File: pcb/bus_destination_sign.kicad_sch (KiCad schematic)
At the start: 34 parts, among them J1 USB_C_Receptacle_USB2.0_16P, J2 Display Connector Input, J3 SSD1322 30-Pin Connector, U1 ESP32-S3-WROOM-1, U2 AP2112K-3.3, U3 MT3608

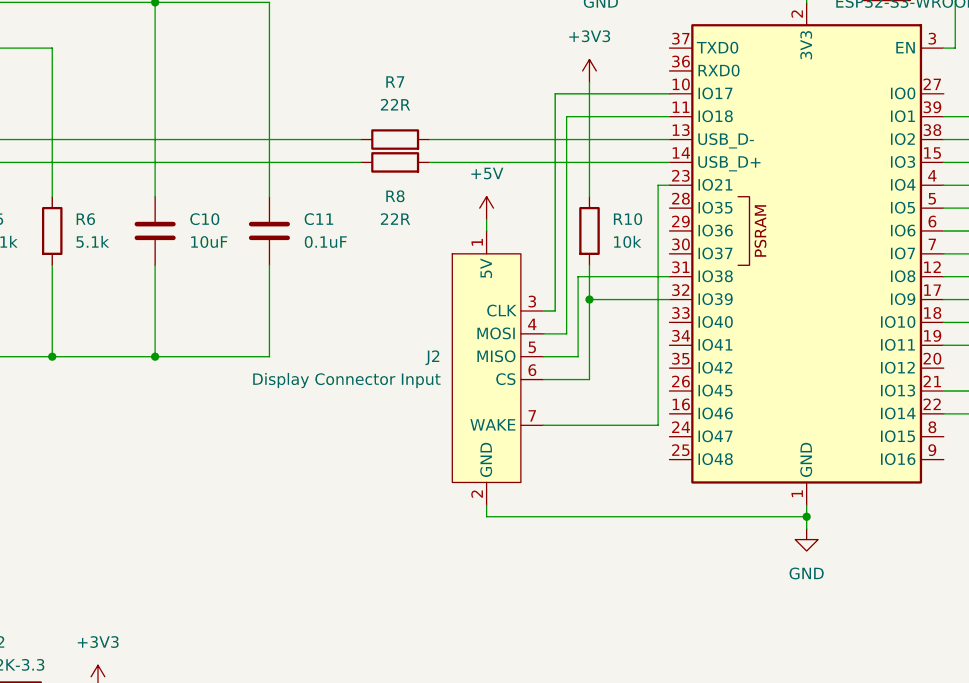
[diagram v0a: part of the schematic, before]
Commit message: Reroute SSD1322 PCB
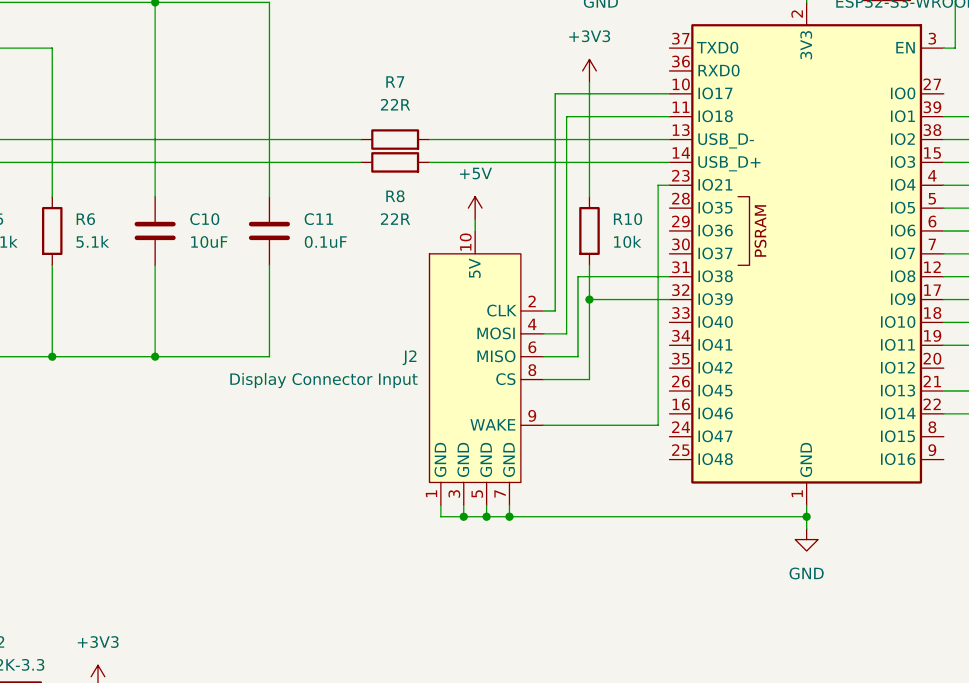
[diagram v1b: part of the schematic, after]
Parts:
- J2: footprint Connector_PinHeader_2.54mm:PinHeader_1x07_P2.54mm_Vertical -> Connector_IDC:IDC-Header_2x05_P2.54mm_Horizontal
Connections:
- net +5V: now also J2.10 (5V); no longer J2.1 (5V)
- net GND: now also J2.1 (GND), J2.3 (GND), J2.5 (GND), J2.7 (GND); no longer J2.2 (GND)
- net at R10.2, U1.32 (IO39): now also J2.8 (CS); no longer J2.6 (CS)
- net at U1.10 (IO17): now also J2.2 (CLK); no longer J2.3 (CLK)
- net at U1.31 (IO38): now also J2.6 (MISO); no longer J2.5 (MISO)
- net at U1.23 (IO21): now also J2.9 (WAKE); no longer J2.7 (WAKE)

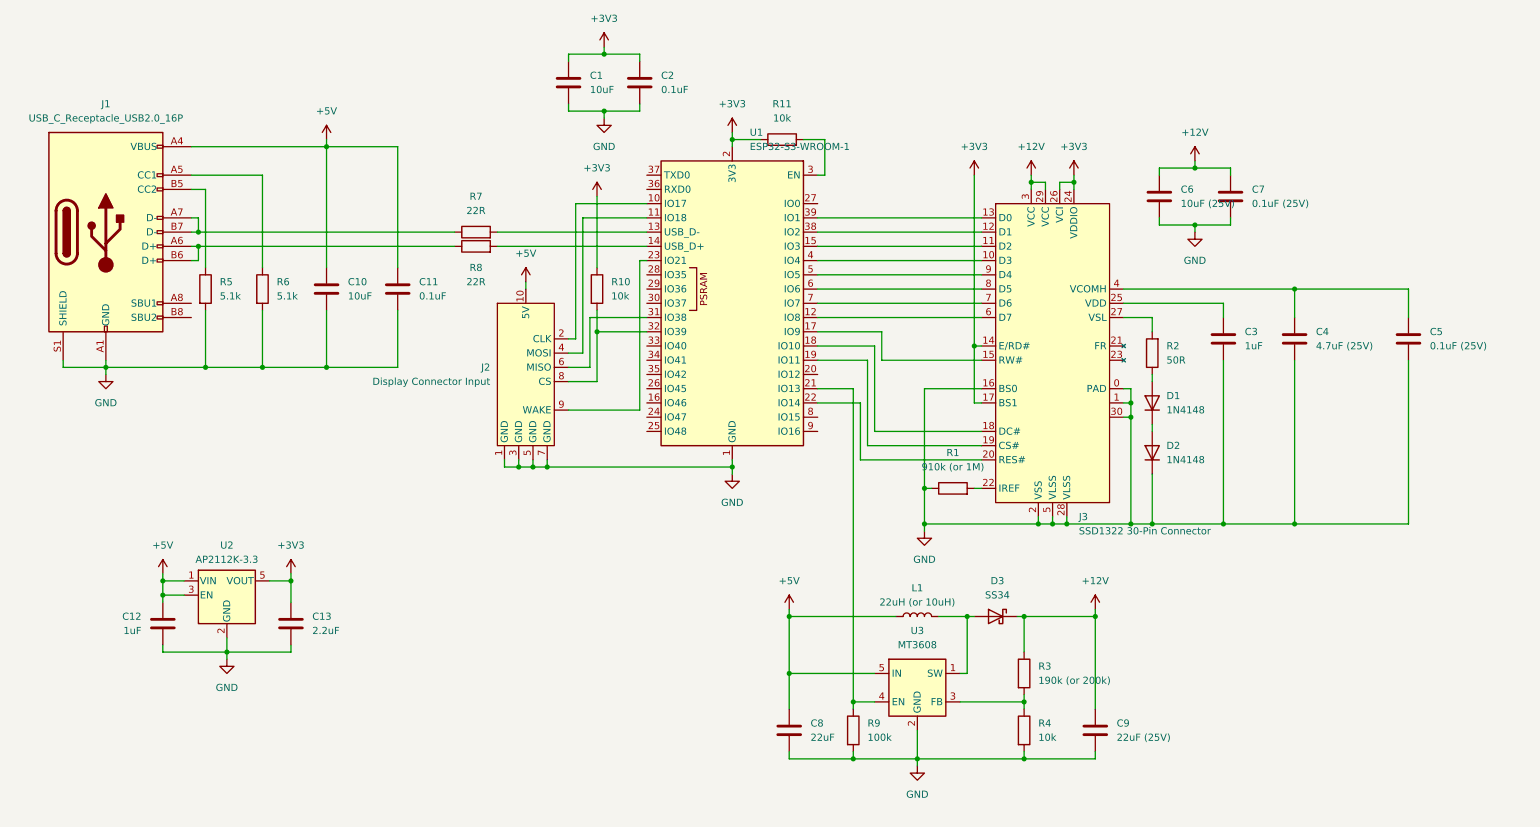
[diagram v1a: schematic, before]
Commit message: Added ESP32 master circuit
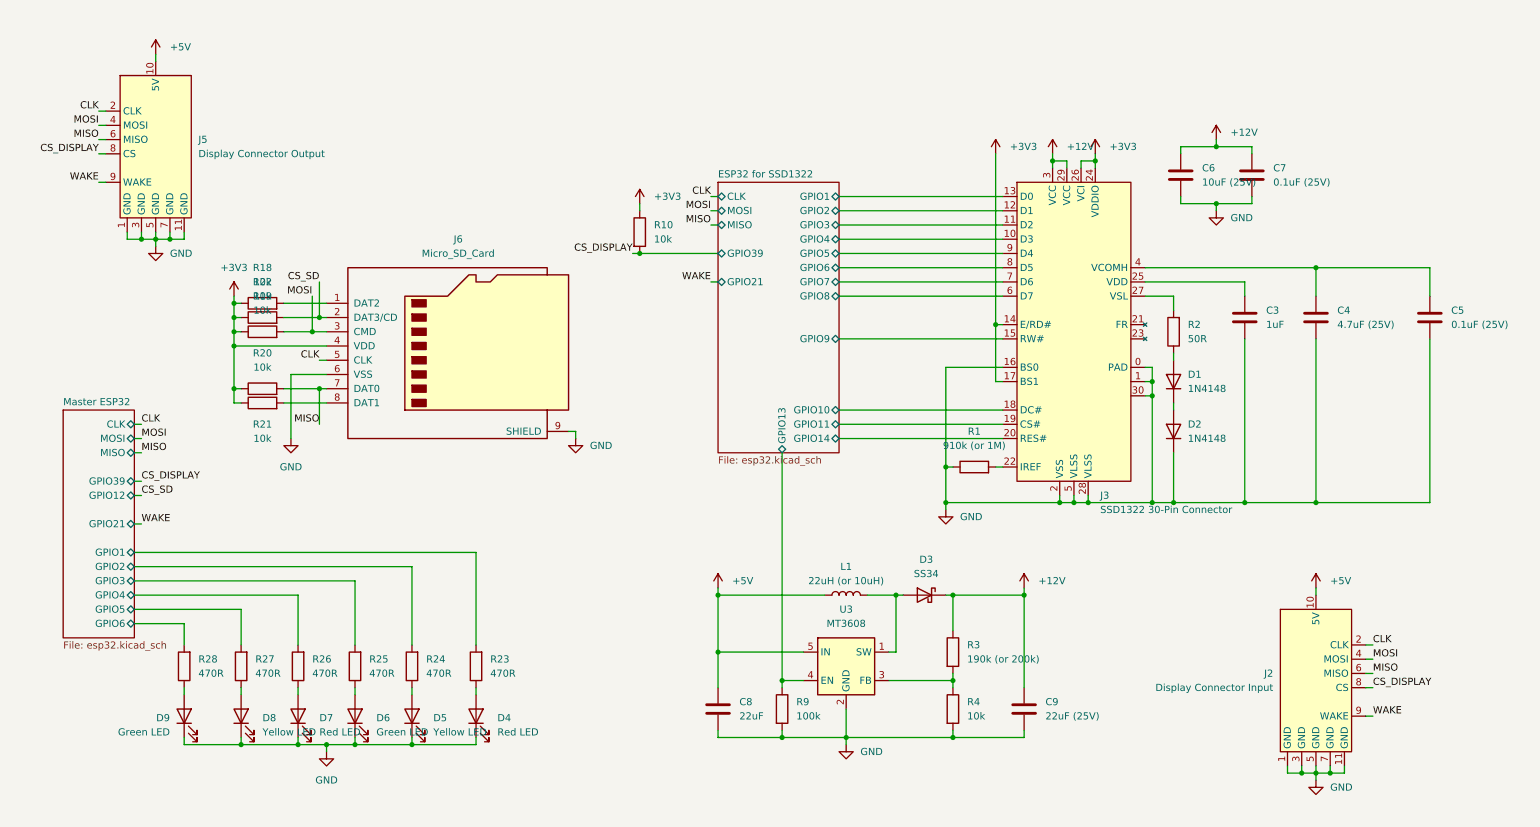
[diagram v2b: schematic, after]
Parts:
- removed C1, C10: 10uF, Capacitor_SMD:C_0603_1608Metric, symbol Device:C
- removed C11, C2: 0.1uF, Capacitor_SMD:C_0603_1608Metric, symbol Device:C
- removed C12: 1uF, Capacitor_SMD:C_0603_1608Metric, symbol Device:C
- removed C13: 2.2uF, Capacitor_SMD:C_0603_1608Metric, symbol Device:C
- removed J1: USB_C_Receptacle_USB2.0_16P, Connector_USB:USB_C_Receptacle_HCTL_HC-TYPE-C-16P-01A, symbol Connector:USB_C_Receptacle_USB2.0_16P
- removed R11: 10k, Resistor_SMD:R_0603_1608Metric, symbol Device:R
- removed R5, R6: 5.1k, Resistor_SMD:R_0603_1608Metric, symbol Device:R
- removed R7, R8: 22R, Resistor_SMD:R_0603_1608Metric, symbol Device:R
- removed U1: ESP32-S3-WROOM-1, RF_Module:ESP32-S3-WROOM-1, symbol RF_Module:ESP32-S3-WROOM-1
- removed U2: AP2112K-3.3, Package_TO_SOT_SMD:SOT-23-5, symbol Regulator_Linear:AP2112K-3.3
- added D4, D7: Red LED, LED_SMD:LED_0603_1608Metric, symbol Device:LED
- added D5, D8: Yellow LED, LED_SMD:LED_0603_1608Metric, symbol Device:LED
- added D6, D9: Green LED, LED_SMD:LED_0603_1608Metric, symbol Device:LED
- added J5: Display Connector Output, Connector_Molex:Molex_PicoBlade_53261-1071_1x10-1MP_P1.25mm_Horizontal, symbol Data Connector:Display_Connector_Output
- added J6: Micro_SD_Card, Connector_Card:microSD_HC_Molex_47219-2001, symbol Connector:Micro_SD_Card
- added R18, R19, R20, R21, R22: 10k, Resistor_SMD:R_0603_1608Metric, symbol Device:R
- added R23, R24, R25, R26, R27, R28: 470R, Resistor_SMD:R_0603_1608Metric, symbol Device:R
- J2: footprint Connector_IDC:IDC-Header_2x05_P2.54mm_Horizontal -> Connector_Molex:Molex_PicoBlade_53261-1071_1x10-1MP_P1.25mm_Horizontal
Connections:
- net +3V3: now also J6.4 (VDD), R18.1, R19.1, R20.1, R21.1, R22.1
- net +5V: now also J5.10 (5V)
- net GND: now also J2.11 (GND), D4.1 (K), D5.1 (K), D6.1 (K), D7.1 (K), D8.1 (K), D9.1 (K), J5.1 (GND), J5.11 (GND), J5.3 (GND), J5.5 (GND), J5.7 (GND), J6.6 (VSS), J6.9 (SHIELD)
- net ESP32 for SSD1322/GPIO4: now reaches J3.10 (D3)
- net ESP32 for SSD1322/GPIO3: now reaches J3.11 (D2)
- net ESP32 for SSD1322/GPIO2: now reaches J3.12 (D1)
- net ESP32 for SSD1322/GPIO1: now reaches J3.13 (D0)
- net ESP32 for SSD1322/GPIO9: now reaches J3.15 (RW#)
- net ESP32 for SSD1322/GPIO10: now reaches J3.18 (DC#)
- net ESP32 for SSD1322/GPIO11: now reaches J3.19 (CS#)
- net ESP32 for SSD1322/GPIO14: now reaches J3.20 (RES#)
- net ESP32 for SSD1322/GPIO8: now reaches J3.6 (D7)
- net ESP32 for SSD1322/GPIO7: now reaches J3.7 (D6)
- net ESP32 for SSD1322/GPIO6: now reaches J3.8 (D5)
- net ESP32 for SSD1322/GPIO5: now reaches J3.9 (D4)
- net CS_DISPLAY: now reaches J2.8 (CS), R10.2
- net CS_DISPLAY: now also J5.8 (CS)
- net CLK: now reaches J2.2 (CLK)
- net CLK: now also J5.2 (CLK), J6.5 (CLK)
- net MOSI: now reaches J2.4 (MOSI)
- net MOSI: now also J5.4 (MOSI), J6.3 (CMD), R19.2
- net ESP32 for SSD1322/GPIO13: now reaches R9.1, U3.4 (EN)
- net WAKE: now reaches J2.9 (WAKE)
- net WAKE: now also J5.9 (WAKE)
- net MISO: now reaches J2.6 (MISO)
- net MISO: now also J5.6 (MISO), J6.7 (DAT0), R20.2
- new net: D9.2 (A), R28.1
- new net: D8.2 (A), R27.1
- new net: D4.2 (A), R23.1
- new net: D5.2 (A), R24.1
- new net: D6.2 (A), R25.1
- new net: D7.2 (A), R26.1
- new net: J6.1 (DAT2), R18.2
- new net: J6.8 (DAT1), R21.2
- new net CS_SD: J6.2 (DAT3/CD), R22.2
- new net Master ESP32/GPIO1: R23.2
- new net Master ESP32/GPIO2: R24.2
- new net Master ESP32/GPIO3: R25.2
- new net Master ESP32/GPIO4: R26.2
- new net Master ESP32/GPIO5: R27.2
- new net Master ESP32/GPIO6: R28.2
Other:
- added sheet ESP32 for SSD1322 (esp32.kicad_sch)
- added sheet Master ESP32 (esp32.kicad_sch)
- moved on the sheet: C3, C4, C5, C6, C7, C8, C9, D1, D2, D3, J3, L1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

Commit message: Updated LED footprints
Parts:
- D4, D5, D6, D7, D8, D9: footprint LED_SMD:LED_0603_1608Metric -> LED_SMD:LED_0805_2012Metric
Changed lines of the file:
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@@
 			)
 		)
-		(property "Footprint" "LED_SMD:LED_0603_1608Metric"
+		(property "Footprint" "LED_SMD:LED_0805_2012Metric"
 			(at 45.72 144.78 0)
 			(effects
@@
 			)
 		)
-		(property "Footprint" "LED_SMD:LED_0603_1608Metric"
+		(property "Footprint" "LED_SMD:LED_0805_2012Metric"
 			(at 55.88 144.78 0)
 			(effects
@@
 			)
 		)
-		(property "Footprint" "LED_SMD:LED_0603_1608Metric"
+		(property "Footprint" "LED_SMD:LED_0805_2012Metric"
 			(at 86.36 144.78 0)
 			(effects
@@
 			)
 		)
-		(property "Footprint" "LED_SMD:LED_0603_1608Metric"
+		(property "Footprint" "LED_SMD:LED_0805_2012Metric"
 			(at 76.2 144.78 0)
 			(effects
@@
 			)
 		)
-		(property "Footprint" "LED_SMD:LED_0603_1608Metric"
+		(property "Footprint" "LED_SMD:LED_0805_2012Metric"
 			(at 97.79 144.78 0)
 			(effects
@@
 			)
 		)
-		(property "Footprint" "LED_SMD:LED_0603_1608Metric"
+		(property "Footprint" "LED_SMD:LED_0805_2012Metric"
 			(at 66.04 144.78 0)
 			(effects

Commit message: Fixed 3.3V connections and SD card orientation
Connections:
- net GND: now also J2.MP (GND), J5.MP (GND); no longer J2.11 (GND), J5.11 (GND)
- net +3V3 renamed Master ESP32/3V3
- net Master ESP32/3V3: no longer J3.14 (E/RD#), J3.17 (BS1), J3.24 (VDDIO), J3.26 (VCI), R10.1
- new net ESP32 for SSD1322/3V3: J3.14 (E/RD#), J3.17 (BS1), J3.24 (VDDIO), J3.26 (VCI), R10.1
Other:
- sheet ESP32 for SSD1322 ports: added 3V3; removed none
- sheet Master ESP32 ports: added 3V3; removed none
- moved on the sheet: D4, J6, R10, R18, R19, R20, R21, R22, R23

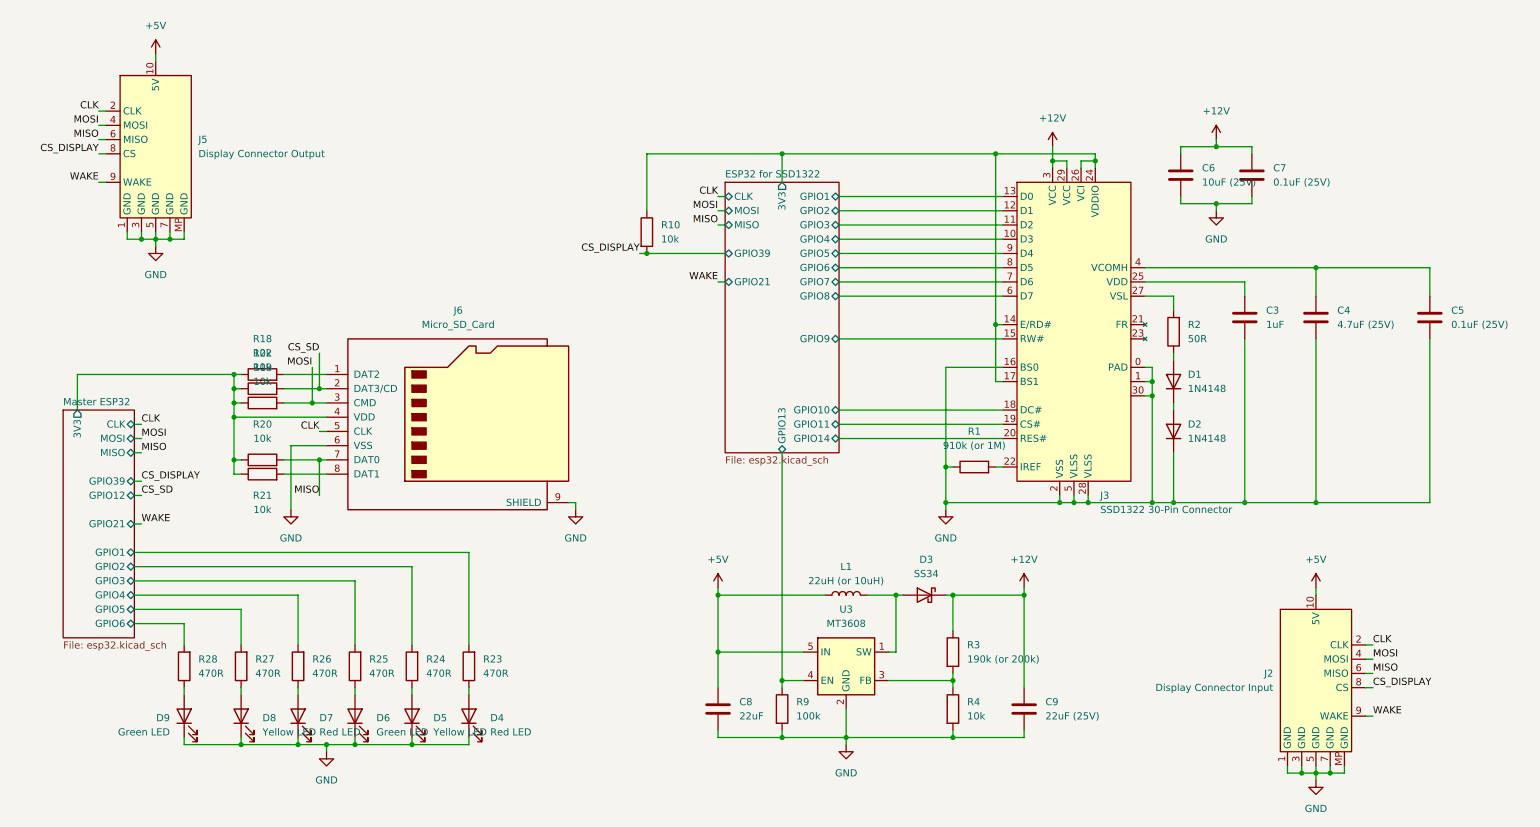
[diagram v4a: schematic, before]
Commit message: Added SSD1327 circuit
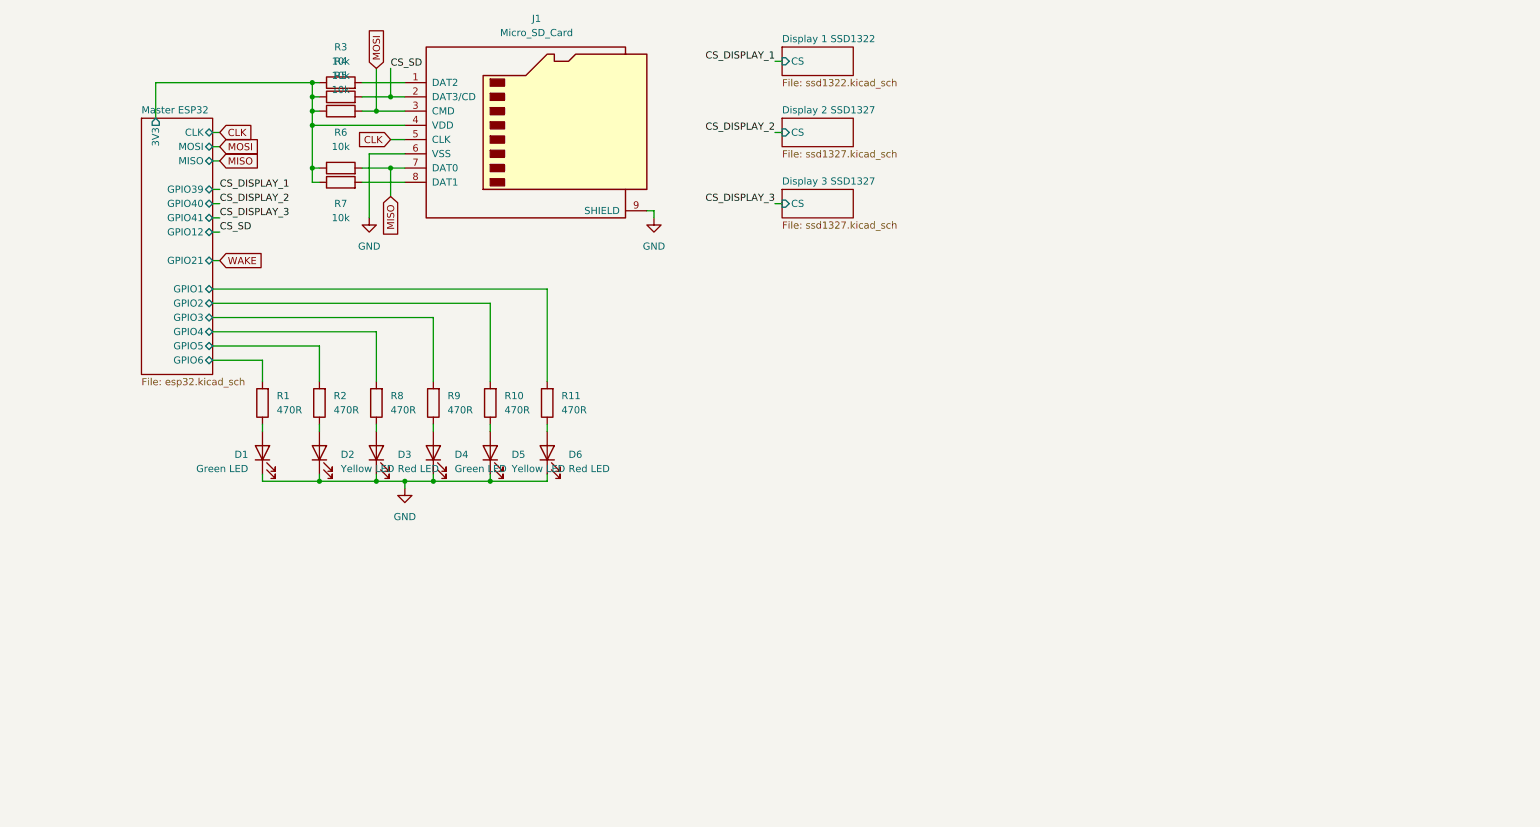
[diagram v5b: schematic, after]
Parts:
- removed C3: 1uF, Capacitor_SMD:C_0603_1608Metric, symbol Device:C
- removed C4: 4.7uF (25V), Capacitor_SMD:C_0603_1608Metric, symbol Device:C
- removed C5, C7: 0.1uF (25V), Capacitor_SMD:C_0603_1608Metric, symbol Device:C
- removed C6: 10uF (25V), Capacitor_SMD:C_0603_1608Metric, symbol Device:C
- removed C8: 22uF, Capacitor_SMD:C_0805_2012Metric, symbol Device:C
- removed C9: 22uF (25V), Capacitor_SMD:C_0805_2012Metric, symbol Device:C
- removed D1, D2: 1N4148, Diode_SMD:D_SOD-123, symbol Diode:1N4148
- removed D3: SS34, Diode_SMD:D_SMA, symbol Diode:SS34
- removed J2: Display Connector Input, Connector_Molex:Molex_PicoBlade_53261-1071_1x10-1MP_P1.25mm_Horizontal, symbol Data Connector:Display_Connector_Input
- removed J3: SSD1322 30-Pin Connector, SSD1322:ssd1322, symbol SSD1322:SSD1322_30-Pin_Connector
- removed J5: Display Connector Output, Connector_Molex:Molex_PicoBlade_53261-1071_1x10-1MP_P1.25mm_Horizontal, symbol Data Connector:Display_Connector_Output
- removed L1: 22uH (or 10uH), Inductor_SMD:L_0603_1608Metric, symbol Device:L
- removed R1: 910k (or 1M), Resistor_SMD:R_0603_1608Metric, symbol Device:R
- removed R10, R4: 10k, Resistor_SMD:R_0603_1608Metric, symbol Device:R
- removed R2: 50R, Resistor_SMD:R_0603_1608Metric, symbol Device:R
- removed R3: 190k (or 200k), Resistor_SMD:R_0603_1608Metric, symbol Device:R
- removed R9: 100k, Resistor_SMD:R_0603_1608Metric, symbol Device:R
- removed U3: MT3608, Package_TO_SOT_SMD:SOT-23-6, symbol Regulator_Switching:MT3608
- renumbered D9 to D1, D8 to D2, D7 to D3, D6 to D4, D4 to D6, J6 to J1, R28 to R1, R24 to R10, R23 to R11, R27 to R2, R18 to R3, R22 to R4, R19 to R5, R20 to R6, R21 to R7, R26 to R8, R25 to R9
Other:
- removed sheet ESP32 for SSD1322
- added sheet Display 1 SSD1322 (ssd1322.kicad_sch)
- added sheet Display 2 SSD1327 (ssd1327.kicad_sch)
- added sheet Display 3 SSD1327 (ssd1327.kicad_sch)
- sheet Master ESP32 ports: added GPIO40, GPIO41; removed none
- moved on the sheet: D1, D2, D3, D4, D5, D6, J1, R1, R10, R11, R2, R3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
